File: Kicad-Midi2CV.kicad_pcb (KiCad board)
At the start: 2 copper layers, 99.7 x 99.7 mm, 78 parts, among them IC1 MCP4725module, IC2 MCP4725module, J1 Doepfer connector, J10 CV4, J11 Gate1, J12 GateConn, J13 Gate2, J14 Gate3, J15 Gate4, J16 I2C_Conn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

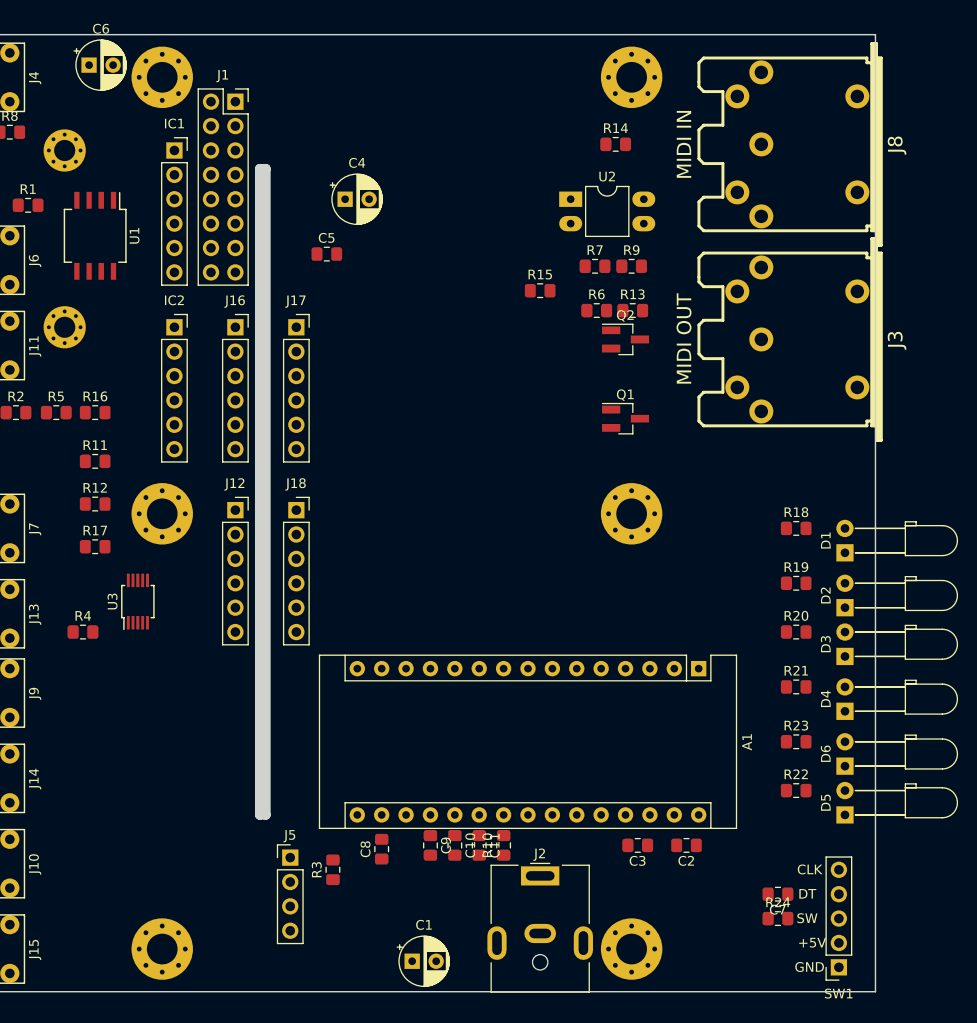
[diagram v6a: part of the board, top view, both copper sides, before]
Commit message: Interconn footprint adj
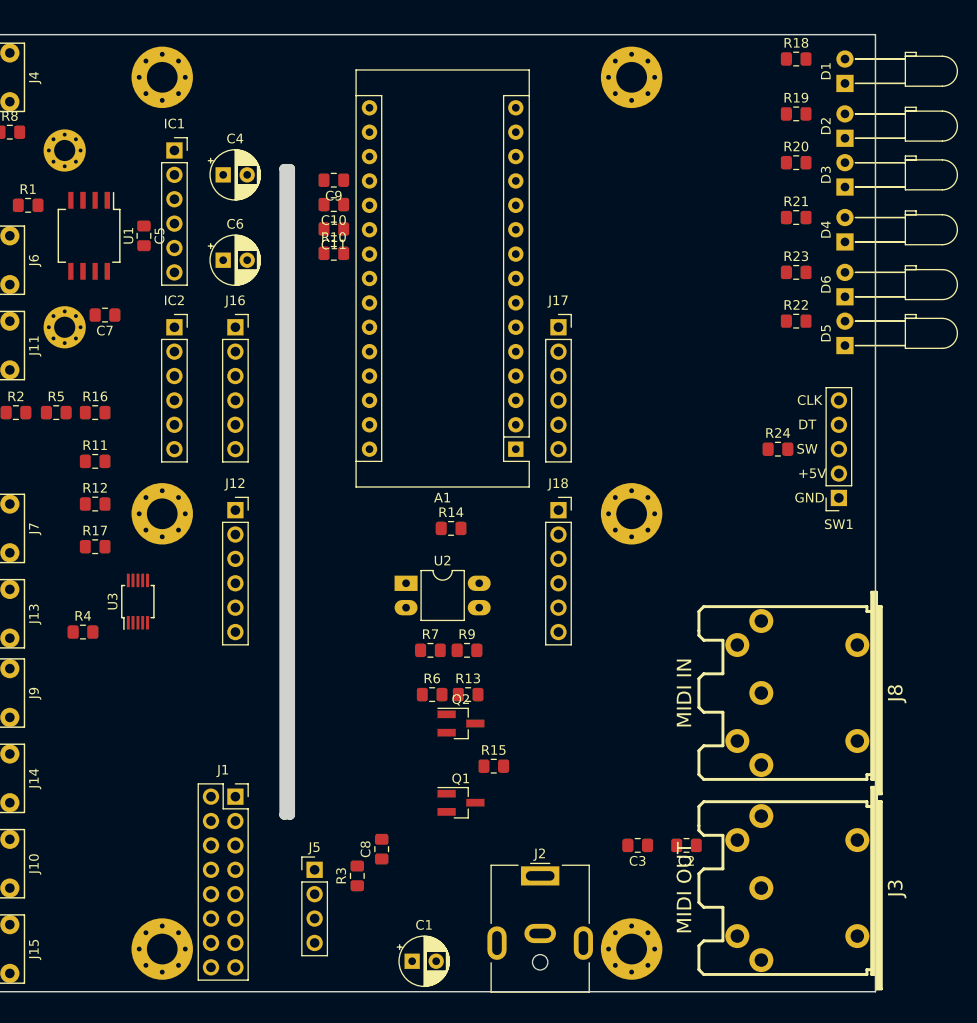
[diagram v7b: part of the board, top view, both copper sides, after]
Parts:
- moved C7 92.5 mm to (44.8, 54.6)
- moved J1 72.4 mm to (58.4, 104.8)
- moved C9 70.0 mm to (68.7, 40.6), turned to 180 degrees
- moved C10 67.9 mm to (68.7, 43.1), turned to 180 degrees
- moved C11 66.0 mm to (68.7, 45.6), turned to 180 degrees
- moved R10 64.2 mm to (68.7, 48.2), turned to 0 degrees
- moved J8 57.2 mm to (116.2, 94.0)
- moved J3 57.1 mm to (116.2, 114.3)
- moved R15 49.8 mm to (85.3, 101.6)
- moved D5 48.9 mm to (121.9, 57.8)
- moved SW1 48.9 mm to (121.3, 73.7)
- moved D2 48.9 mm to (121.9, 36.2)
- moved D3 48.9 mm to (121.9, 41.3)
- moved D4 48.9 mm to (121.9, 47.0)
- moved R22 48.9 mm to (116.8, 55.2)
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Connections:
- J16 pad 2: /SDA -> /SCL
- J16 pad 3: /SCL -> /SDA
- J17 pad 2: /SDA -> /SCL
- J17 pad 3: /SCL -> /SDA
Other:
- outline, holes or cut-outs redrawn
